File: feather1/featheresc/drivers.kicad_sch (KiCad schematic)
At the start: 10 parts, among them J3 PHASE2, J4 PHASE1, Q1 NCEP40T20ALL, Q2 NCEP40T20ALL, Q3 NCEP40T20ALL, Q4 NCEP40T20ALL

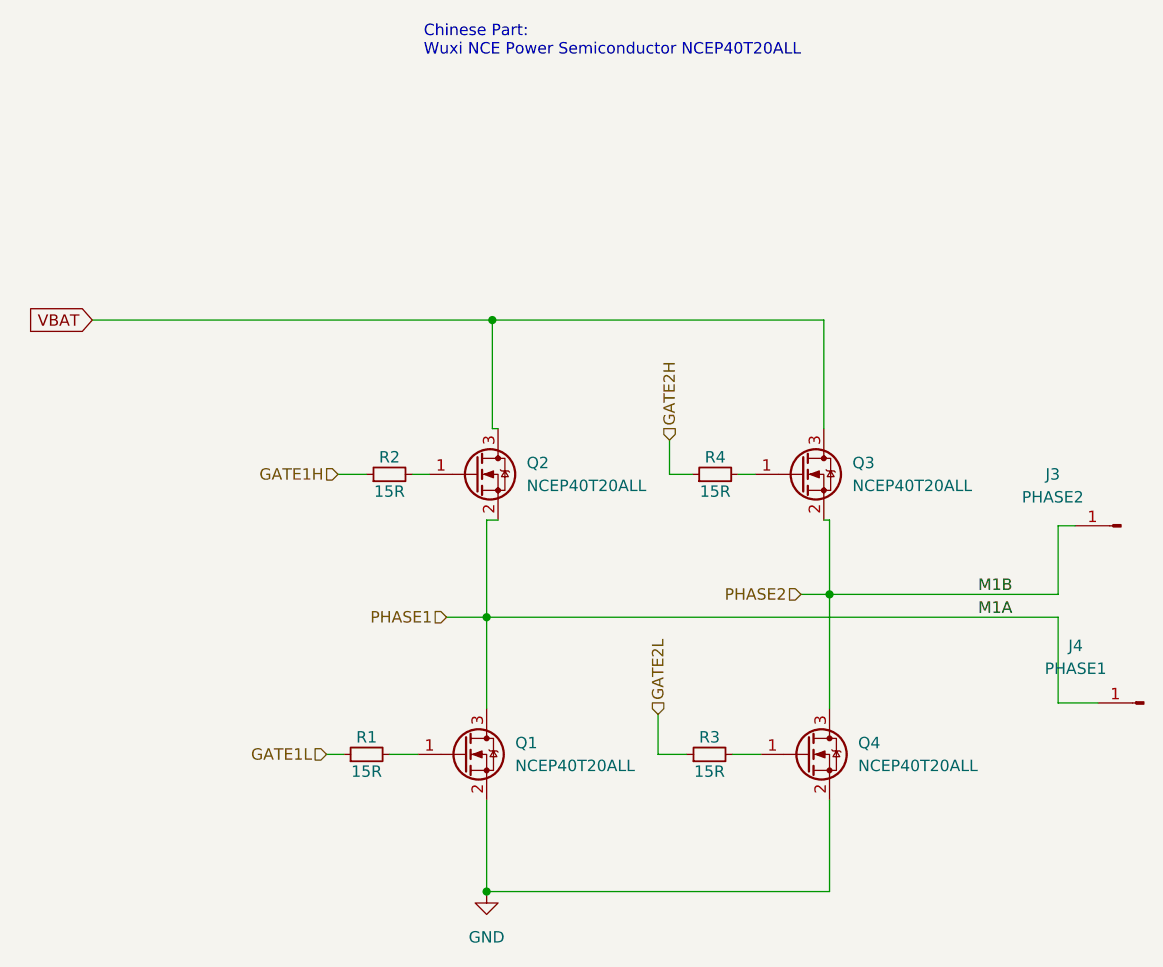
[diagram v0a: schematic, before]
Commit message: Feather ESC power board
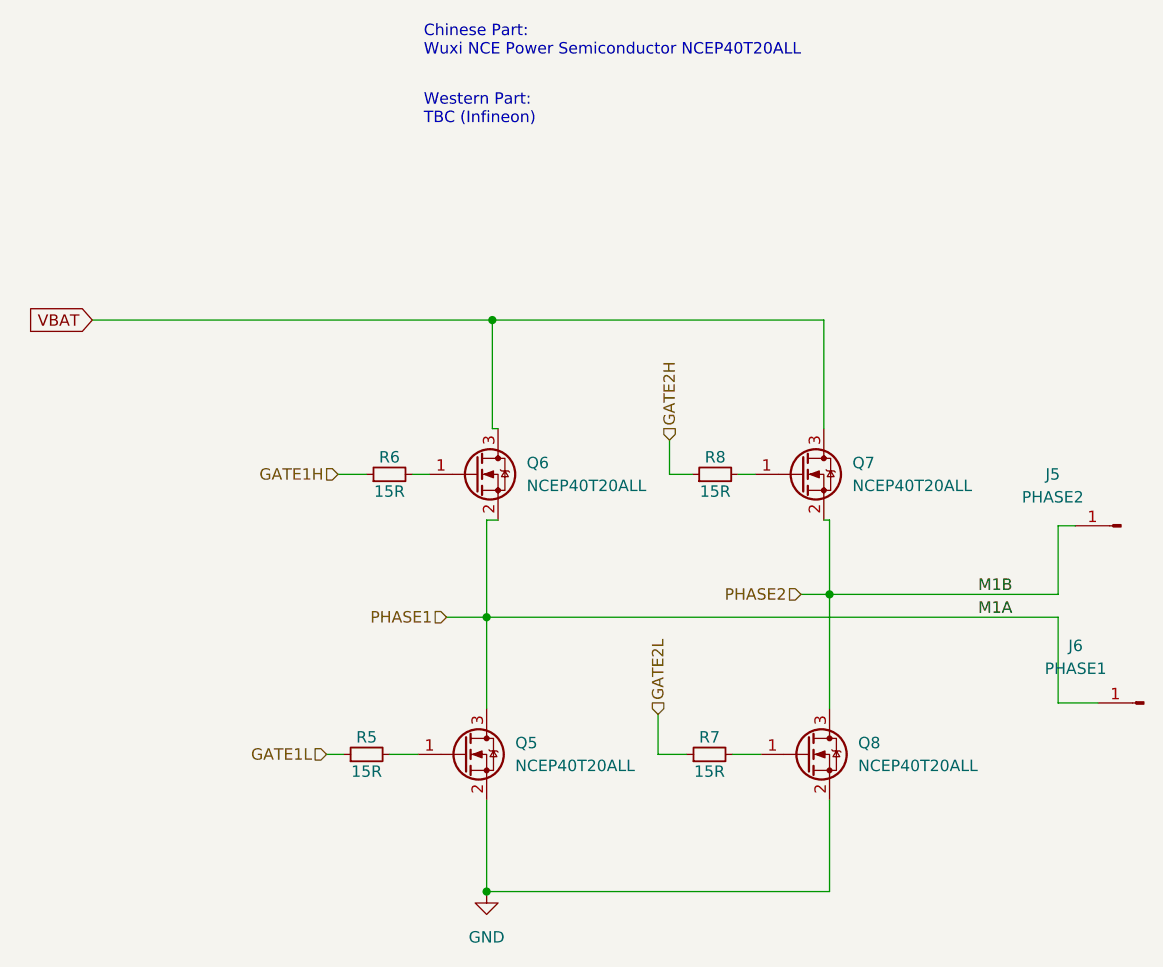
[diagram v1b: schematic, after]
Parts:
- renumbered J3 to J5, J4 to J6, Q1 to Q5, Q2 to Q6, Q3 to Q7, Q4 to Q8, R1 to R5, R2 to R6, R3 to R7, R4 to R8
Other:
- note added: "Western Part: TBC (Infineon)"
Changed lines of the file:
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@@
 (kicad_sch (version 20210621) (generator eeschema)
   (paper "A4")
+  (junction (at 139.065 97.155) (diameter 0) (color 0 0 0 0))
   (junction (at 177.165 94.615) (diameter 0) (color 0 0 0 0))
   (junction (at 139.065 127.635) (diameter 0) (color 0 0 0 0))
   (junction (at 139.7 64.135) (diameter 0) (color 0 0 0 0))
-  (junction (at 139.065 97.155) (diameter 0) (color 0 0 0 0))
   (wire (pts (xy 95.25 64.135) (xy 139.7 64.135))
     (stroke (width 0) (type default) (color 0 0 0 0))
@@
     (effects (font (size 1.27 1.27)) (justify left bottom))
   )
+  (text "Western Part:\nTBC (Infineon)" (at 132.08 42.545 0)
+    (effects (font (size 1.27 1.27)) (justify left bottom))
+  )
   (label "M1B" (at 193.675 94.615 0)
     (effects (font (size 1.27 1.27)) (justify left bottom))
@@
   (symbol (lib_id "Transistor_FET:IPT012N08N5") (at 173.99 81.28 0)
     (in_bom yes) (on_board yes) (fields_autoplaced)
-    (property "Reference" "Q3" (id 0) (at 179.705 80.0099 0)
+    (property "Reference" "Q7" (id 0) (at 179.705 80.0099 0)
       (effects (font (size 1.27 1.27)) (justify left))
     )
@@
   (symbol (lib_id "Transistor_FET:IPT012N08N5") (at 174.625 112.395 0)
     (in_bom yes) (on_board yes) (fields_autoplaced)
-    (property "Reference" "Q4" (id 0) (at 180.34 111.1249 0)
+    (property "Reference" "Q8" (id 0) (at 180.34 111.1249 0)
       (effects (font (size 1.27 1.27)) (justify left))
     )
@@
   (symbol (lib_id "power:GND") (at 139.065 127.635 0)
     (in_bom yes) (on_board yes) (fields_autoplaced)
-    (property "Reference" "#PWR02" (id 0) (at 139.065 133.985 0)
+    (property "Reference" "#PWR03" (id 0) (at 139.065 133.985 0)
       (effects (font (size 1.27 1.27)) hide)
     )
@@
   (symbol (lib_id "Connector:Conn_01x01_Male") (at 212.09 106.68 0) (mirror y)
     (in_bom yes) (on_board yes) (fields_autoplaced)
-    (property "Reference" "J4" (id 0) (at 204.508 100.33 0))
+    (property "Reference" "J6" (id 0) (at 204.508 100.33 0))
     (property "Value" "PHASE1" (id 1) (at 204.508 102.87 0))
     (property "Footprint" "featheresc:screw_lug_terminal" (id 2) (at 212.09 106.68 0)
@@
   (symbol (lib_id "Transistor_FET:IPT012N08N5") (at 137.795 81.28 0)
     (in_bom yes) (on_board yes) (fields_autoplaced)
-    (property "Reference" "Q2" (id 0) (at 143.51 80.0099 0)
+    (property "Reference" "Q6" (id 0) (at 143.51 80.0099 0)
       (effects (font (size 1.27 1.27)) (justify left))
     )
@@
   (symbol (lib_id "Device:R_Small") (at 128.27 81.28 90)
     (in_bom yes) (on_board yes)
-    (property "Reference" "R2" (id 0) (at 128.27 79.375 90))
+    (property "Reference" "R6" (id 0) (at 128.27 79.375 90))
     (property "Value" "15R" (id 1) (at 128.27 83.185 90))
     (property "Footprint" "Resistor_THT:R_Axial_DIN0207_L6.3mm_D2.5mm_P15.24mm_Horizontal" (id 2) (at 128.27 81.28 0)
@@
   (symbol (lib_id "Device:R_Small") (at 164.465 81.28 90)
     (in_bom yes) (on_board yes)
-    (property "Reference" "R4" (id 0) (at 164.465 79.375 90))
+    (property "Reference" "R8" (id 0) (at 164.465 79.375 90))
     (property "Value" "15R" (id 1) (at 164.465 83.185 90))
     (property "Footprint" "Resistor_THT:R_Axial_DIN0207_L6.3mm_D2.5mm_P15.24mm_Horizontal" (id 2) (at 164.465 81.28 0)
@@
   (symbol (lib_id "Transistor_FET:IPT012N08N5") (at 136.525 112.395 0)
     (in_bom yes) (on_board yes) (fields_autoplaced)
-    (property "Reference" "Q1" (id 0) (at 142.24 111.1249 0)
+    (property "Reference" "Q5" (id 0) (at 142.24 111.1249 0)
       (effects (font (size 1.27 1.27)) (justify left))
     )
@@
   (symbol (lib_id "Device:R_Small") (at 163.83 112.395 90)
     (in_bom yes) (on_board yes)
-    (property "Reference" "R3" (id 0) (at 163.83 110.49 90))
+    (property "Reference" "R7" (id 0) (at 163.83 110.49 90))
     (property "Value" "15R" (id 1) (at 163.83 114.3 90))
     (property "Footprint" "Resistor_THT:R_Axial_DIN0207_L6.3mm_D2.5mm_P15.24mm_Horizontal" (id 2) (at 163.83 112.395 0)
@@
   (symbol (lib_id "Connector:Conn_01x01_Male") (at 209.55 86.995 0) (mirror y)
     (in_bom yes) (on_board yes) (fields_autoplaced)
-    (property "Reference" "J3" (id 0) (at 201.968 81.28 0))
+    (property "Reference" "J5" (id 0) (at 201.968 81.28 0))
     (property "Value" "PHASE2" (id 1) (at 201.968 83.82 0))
     (property "Footprint" "featheresc:screw_lug_terminal" (id 2) (at 209.55 86.995 0)
@@
   (symbol (lib_id "Device:R_Small") (at 125.73 112.395 90)
     (in_bom yes) (on_board yes)
-    (property "Reference" "R1" (id 0) (at 125.73 110.49 90))
+    (property "Reference" "R5" (id 0) (at 125.73 110.49 90))
     (property "Value" "15R" (id 1) (at 125.73 114.3 90))
     (property "Footprint" "Resistor_THT:R_Axial_DIN0207_L6.3mm_D2.5mm_P15.24mm_Horizontal" (id 2) (at 125.73 112.395 0)
